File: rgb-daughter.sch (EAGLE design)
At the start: 103 parts

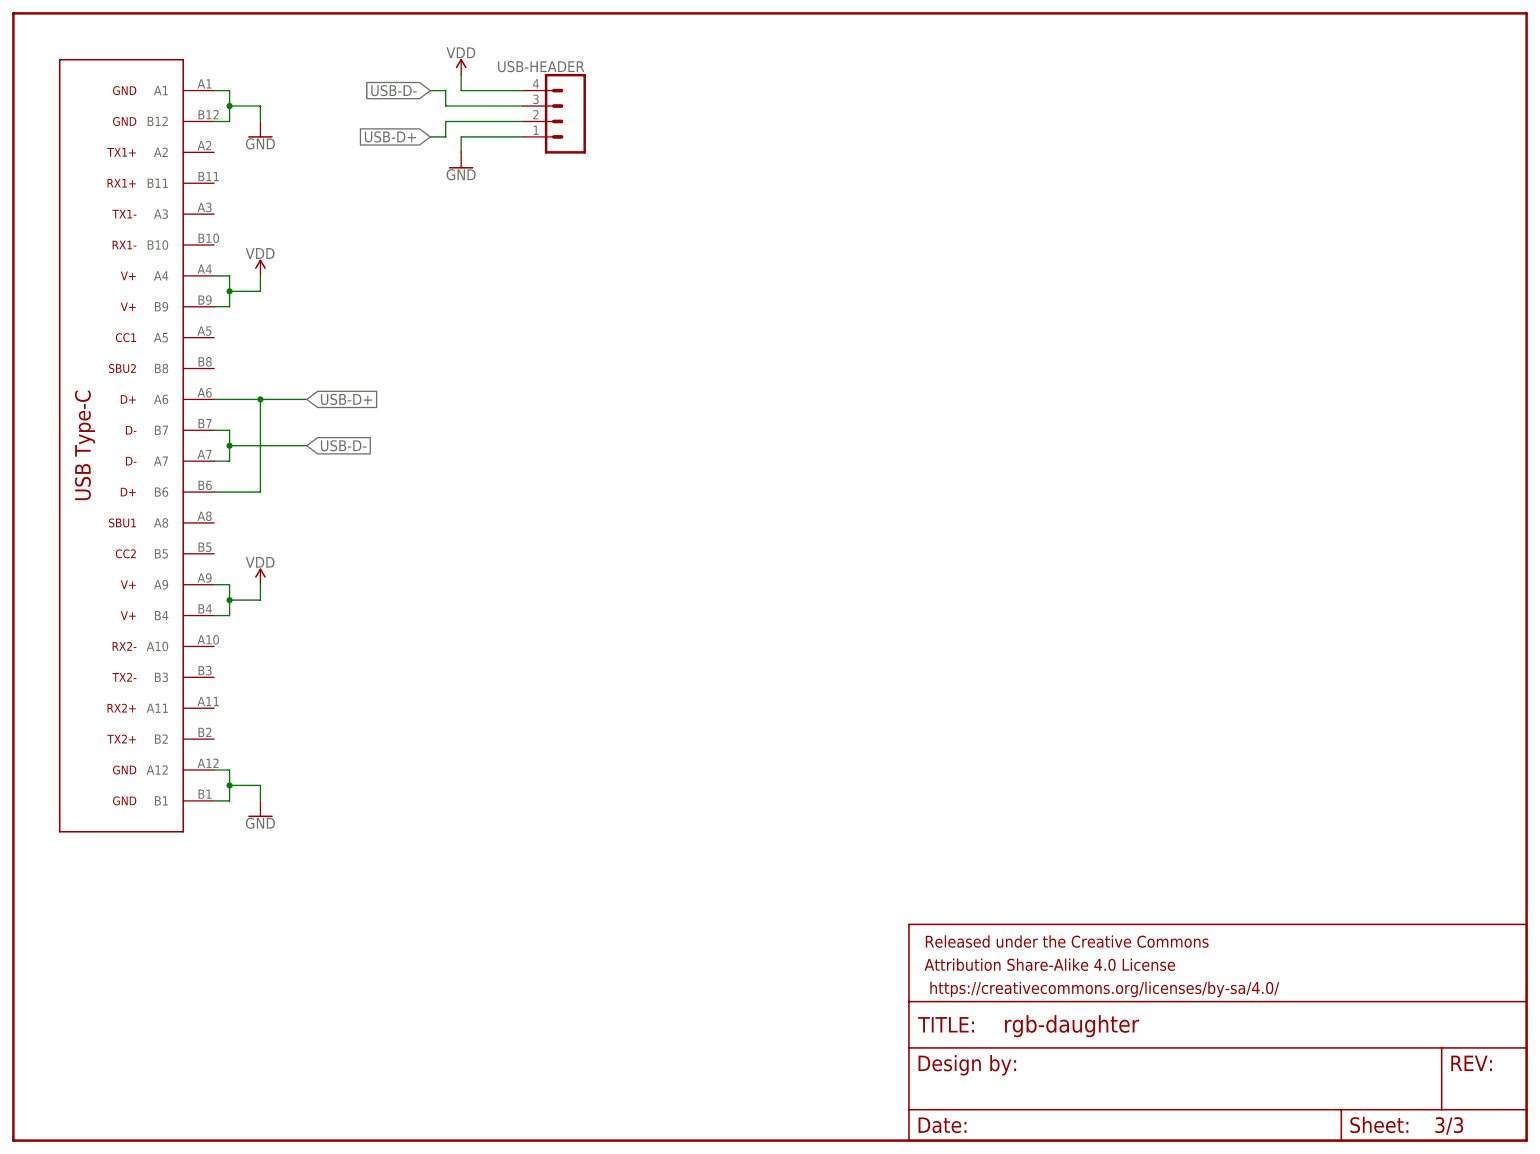
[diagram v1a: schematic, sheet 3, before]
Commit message: 👽 update for new USB-C package
- connect new pins on USB-C
- move USB-C package to match placement in case
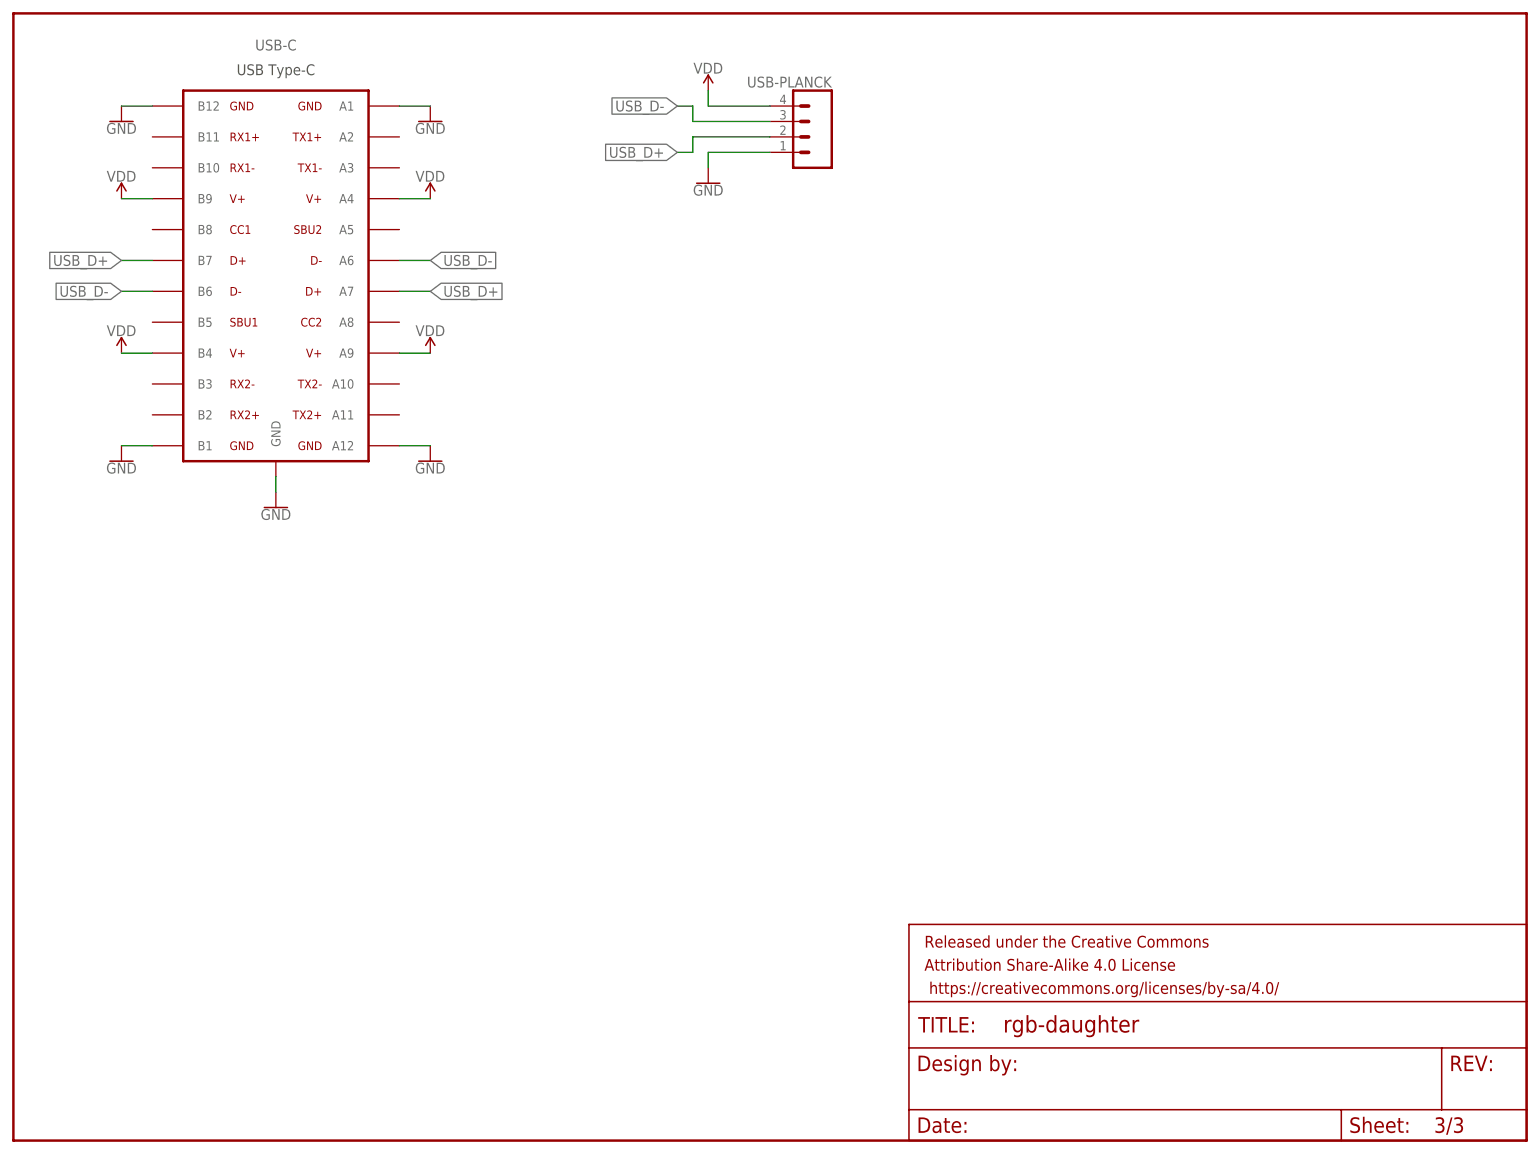
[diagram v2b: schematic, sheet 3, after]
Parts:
- removed U$1: USB-TYPE-CDX07S024JJ3R1300, usb:USB-TYPE-CDX07S024JJ3R1300
- removed USB-HEADER: (no value), SparkFun-Connectors:CONN_041.27MM
- added USB-C: USB-TYPE-CDX07S024JJ3R1300, usb:USB-TYPE-CDX07S024JJ3R1300
- added USB-PLANCK: (no value), SparkFun-Connectors:CONN_041.27MM
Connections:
- removed net USB-D+: U$1.A6, U$1.B6, USB-HEADER.2
- removed net USB-D-: U$1.A7, U$1.B7, USB-HEADER.3
- new net USB_D+: USB-C.A7, USB-C.B7, USB-PLANCK.2
- new net USB_D-: USB-C.A6, USB-C.B6, USB-PLANCK.3
- net GND: now also USB-C.A1, USB-C.A12, USB-C.B1, USB-C.B12, USB-C.GND, USB-PLANCK.1; no longer U$1.A1, U$1.A12, U$1.B1, U$1.B12, USB-HEADER.1
- net VDD: now also USB-C.A4, USB-C.A9, USB-C.B4, USB-C.B9, USB-PLANCK.4; no longer U$1.A4, U$1.A9, U$1.B4, U$1.B9, USB-HEADER.4

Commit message: 🐛 fix LED numbering
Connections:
- removed net N$22 (its old number): LED24.DO, LED25.DI
- new net N$47: LED47.DO, LED48.DI
- net DO: now also LED24.DO, LED25.DI; no longer LED24.DI, LED48.DO
- net N$25: now also LED24.DI; no longer LED48.DI

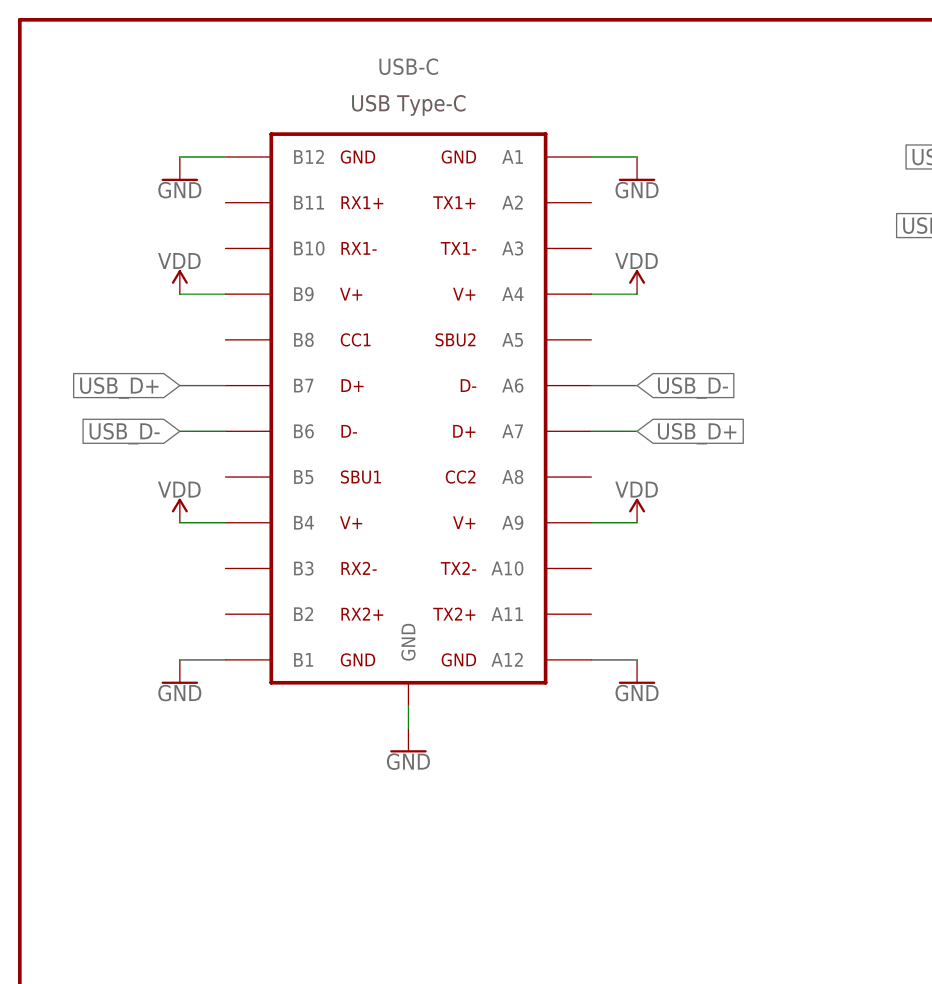
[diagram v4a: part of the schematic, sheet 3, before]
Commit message: 🐛 fix USB-C pad layout
- D+ and D- were swapped
- simplify USB-C symbol
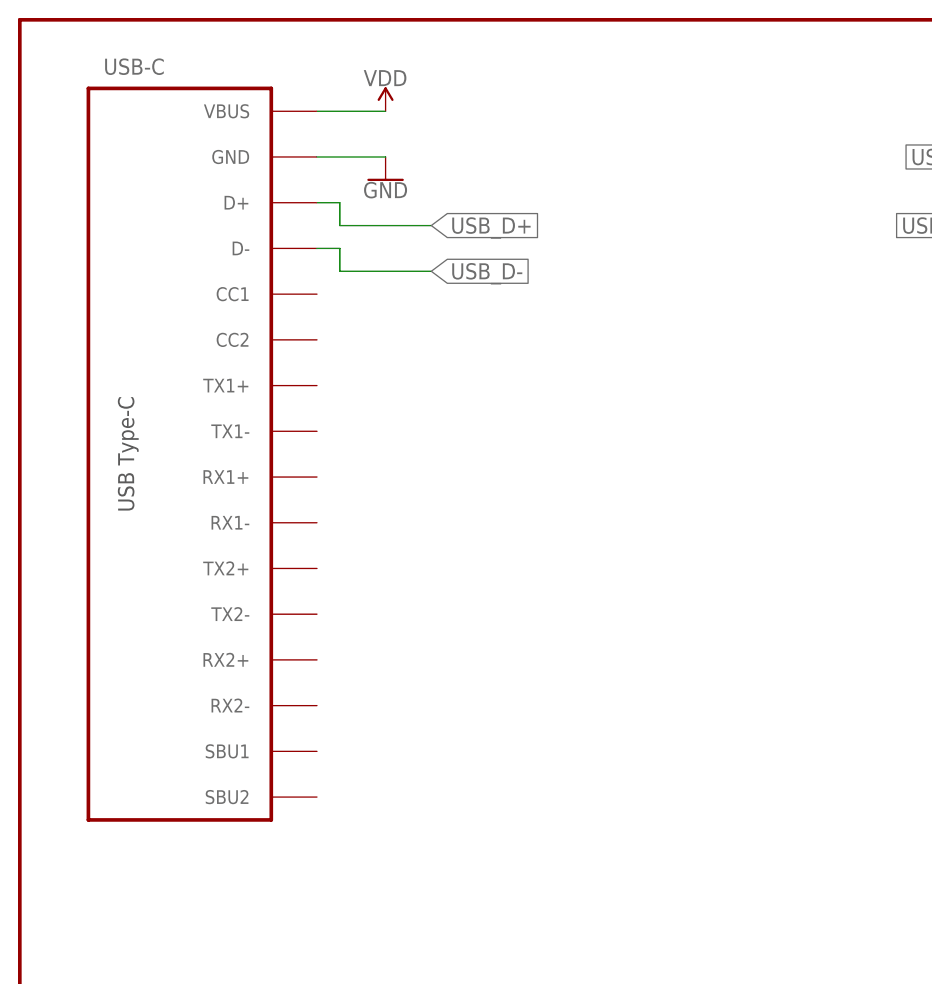
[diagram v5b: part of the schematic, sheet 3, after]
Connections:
- net GND: no longer USB-C.A1, USB-C.A12, USB-C.B1, USB-C.B12
- net USB_D+: now also USB-C.D+; no longer USB-C.A7, USB-C.B7
- net USB_D-: now also USB-C.D-; no longer USB-C.A6, USB-C.B6
- net VDD: now also USB-C.VBUS; no longer USB-C.A4, USB-C.A9, USB-C.B4, USB-C.B9
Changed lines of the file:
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@@
 <part name="SUPPLY52" library="SparkFun-PowerSymbols" library_urn="urn:adsk.eagle:library:530" deviceset="VDD" device=""/>
 <part name="SUPPLY50" library="SparkFun-PowerSymbols" library_urn="urn:adsk.eagle:library:530" deviceset="VDD" device=""/>
-<part name="SUPPLY51" library="SparkFun-PowerSymbols" library_urn="urn:adsk.eagle:library:530" deviceset="VDD" device=""/>
-<part name="SUPPLY53" library="SparkFun-PowerSymbols" library_urn="urn:adsk.eagle:library:530" deviceset="VDD" device=""/>
-<part name="SUPPLY54" library="SparkFun-PowerSymbols" library_urn="urn:adsk.eagle:library:530" deviceset="VDD" device=""/>
-<part name="GND50" library="SparkFun-PowerSymbols" library_urn="urn:adsk.eagle:library:530" deviceset="GND" device=""/>
-<part name="GND51" library="SparkFun-PowerSymbols" library_urn="urn:adsk.eagle:library:530" deviceset="GND" device=""/>
-<part name="GND53" library="SparkFun-PowerSymbols" library_urn="urn:adsk.eagle:library:530" deviceset="GND" device=""/>
-<part name="GND54" library="SparkFun-PowerSymbols" library_urn="urn:adsk.eagle:library:530" deviceset="GND" device=""/>
 <part name="GND55" library="SparkFun-PowerSymbols" library_urn="urn:adsk.eagle:library:530" deviceset="GND" device=""/>
 </parts>
@@
 <instance part="FRAME3" gate="G$1" x="0" y="0"/>
 <instance part="FRAME3" gate="V" x="147.32" y="0"/>
-<instance part="USB-C" gate="G$1" x="43.18" y="142.24"/>
+<instance part="USB-C" gate="G$1" x="15.24" y="137.16"/>
 <instance part="USB-PLANCK" gate="G$1" x="129.54" y="165.1" rot="MR0"/>
 <instance part="GND52" gate="1" x="114.3" y="157.48"/>
 <instance part="SUPPLY52" gate="VDD" x="114.3" y="172.72"/>
-<instance part="SUPPLY50" gate="VDD" x="68.58" y="154.94"/>
-<instance part="SUPPLY51" gate="VDD" x="17.78" y="154.94"/>
-<instance part="SUPPLY53" gate="VDD" x="68.58" y="129.54"/>
-<instance part="SUPPLY54" gate="VDD" x="17.78" y="129.54"/>
-<instance part="GND50" gate="1" x="68.58" y="111.76"/>
-<instance part="GND51" gate="1" x="17.78" y="111.76"/>
-<instance part="GND53" gate="1" x="68.58" y="167.64"/>
-<instance part="GND54" gate="1" x="17.78" y="167.64"/>
-<instance part="GND55" gate="1" x="43.18" y="104.14"/>
+<instance part="SUPPLY50" gate="VDD" x="40.64" y="175.26"/>
+<instance part="GND55" gate="1" x="40.64" y="167.64"/>
 </instances>
 <busses>
@@
 </segment>
 <segment>
-<pinref part="USB-C" gate="G$1" pin="A12"/>
-<wire x1="63.5" y1="114.3" x2="68.58" y2="114.3" width="0.1524" layer="91"/>
-<pinref part="GND50" gate="1" pin="GND"/>
-</segment>
-<segment>
-<pinref part="USB-C" gate="G$1" pin="B1"/>
-<wire x1="22.86" y1="114.3" x2="17.78" y2="114.3" width="0.1524" layer="91"/>
-<pinref part="GND51" gate="1" pin="GND"/>
-</segment>
-<segment>
-<pinref part="USB-C" gate="G$1" pin="A1"/>
-<wire x1="63.5" y1="170.18" x2="68.58" y2="170.18" width="0.1524" layer="91"/>
-<pinref part="GND53" gate="1" pin="GND"/>
-</segment>
-<segment>
-<pinref part="USB-C" gate="G$1" pin="B12"/>
-<wire x1="22.86" y1="170.18" x2="17.78" y2="170.18" width="0.1524" layer="91"/>
-<pinref part="GND54" gate="1" pin="GND"/>
-</segment>
-<segment>
 <pinref part="USB-C" gate="G$1" pin="GND"/>
-<wire x1="43.18" y1="109.22" x2="43.18" y2="106.68" width="0.1524" layer="91"/>
+<wire x1="33.02" y1="170.18" x2="40.64" y2="170.18" width="0.1524" layer="91"/>
 <pinref part="GND55" gate="1" pin="GND"/>
 </segment>
@@
 </segment>
 <segment>
-<pinref part="USB-C" gate="G$1" pin="A4"/>
-<wire x1="63.5" y1="154.94" x2="68.58" y2="154.94" width="0.1524" layer="91"/>
+<pinref part="USB-C" gate="G$1" pin="VBUS"/>
 <pinref part="SUPPLY50" gate="VDD" pin="VDD"/>
-</segment>
-<segment>
-<pinref part="USB-C" gate="G$1" pin="B9"/>
-<wire x1="22.86" y1="154.94" x2="17.78" y2="154.94" width="0.1524" layer="91"/>
-<pinref part="SUPPLY51" gate="VDD" pin="VDD"/>
-</segment>
-<segment>
-<pinref part="USB-C" gate="G$1" pin="A9"/>
-<wire x1="63.5" y1="129.54" x2="68.58" y2="129.54" width="0.1524" layer="91"/>
-<pinref part="SUPPLY53" gate="VDD" pin="VDD"/>
-</segment>
-<segment>
-<pinref part="USB-C" gate="G$1" pin="B4"/>
-<wire x1="22.86" y1="129.54" x2="17.78" y2="129.54" width="0.1524" layer="91"/>
-<pinref part="SUPPLY54" gate="VDD" pin="VDD"/>
+<wire x1="33.02" y1="175.26" x2="40.64" y2="175.26" width="0.1524" layer="91"/>
 </segment>
 </net>
 <net name="USB_D-" class="0">
-<segment>
-<pinref part="USB-C" gate="G$1" pin="A6"/>
-<wire x1="63.5" y1="144.78" x2="68.58" y2="144.78" width="0.1524" layer="91"/>
-<label x="68.58" y="144.78" size="1.778" layer="95" xref="yes"/>
-</segment>
-<segment>
-<pinref part="USB-C" gate="G$1" pin="B6"/>
-<wire x1="22.86" y1="139.7" x2="17.78" y2="139.7" width="0.1524" layer="91"/>
-<label x="17.78" y="139.7" size="1.778" layer="95" rot="MR0" xref="yes"/>
-</segment>
 <segment>
 <pinref part="USB-PLANCK" gate="G$1" pin="3"/>
@@
 <label x="109.22" y="170.18" size="1.778" layer="95" rot="MR0" xref="yes"/>
 </segment>
+<segment>
+<pinref part="USB-C" gate="G$1" pin="D-"/>
+<wire x1="33.02" y1="160.02" x2="35.56" y2="160.02" width="0.1524" layer="91"/>
+<wire x1="35.56" y1="160.02" x2="35.56" y2="157.48" width="0.1524" layer="91"/>
+<wire x1="35.56" y1="157.48" x2="45.72" y2="157.48" width="0.1524" layer="91"/>
+<label x="45.72" y="157.48" size="1.778" layer="95" xref="yes"/>
+</segment>
 </net>
 <net name="USB_D+" class="0">
-<segment>
-<pinref part="USB-C" gate="G$1" pin="A7"/>
-<wire x1="63.5" y1="139.7" x2="68.58" y2="139.7" width="0.1524" layer="91"/>
-<label x="68.58" y="139.7" size="1.778" layer="95" xref="yes"/>
-</segment>
-<segment>
-<pinref part="USB-C" gate="G$1" pin="B7"/>
-<wire x1="22.86" y1="144.78" x2="17.78" y2="144.78" width="0.1524" layer="91"/>
-<label x="17.78" y="144.78" size="1.778" layer="95" rot="MR0" xref="yes"/>
-</segment>
 <segment>
 <pinref part="USB-PLANCK" gate="G$1" pin="2"/>
@@
 <label x="109.22" y="162.56" size="1.778" layer="95" rot="MR0" xref="yes"/>
 </segment>
-</net>
+<segment>
+<pinref part="USB-C" gate="G$1" pin="D+"/>
+<wire x1="33.02" y1="165.1" x2="35.56" y2="165.1" width="0.1524" layer="91"/>
+<wire x1="35.56" y1="165.1" x2="35.56" y2="162.56" width="0.1524" layer="91"/>
+<wire x1="35.56" y1="162.56" x2="45.72" y2="162.56" width="0.1524" layer="91"/>
+<label x="45.72" y="162.56" size="1.778" layer="95" xref="yes"/>
+</segment>
+</net>
